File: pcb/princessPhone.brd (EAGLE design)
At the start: 83.8 x 53 mm, 75 parts, among them IC1 OPA2134UA, P2 TC2030-MCP-NL, Q1 2N7002K, SW3 LL1105BF250Q, SW4 LL1105BF250Q, SW5 LL1105BF250Q, SW6 LL1105BF250Q, U1 AG1170-S3-VERTICAL, U2 PI32MX170D-PT, U3 BLUETOOTH-RN-52, U4 V_REG_LD1085D2, X1 22-23-2041, X2 XRJK-S-01-6-4-0-9M2, X3 USB_MICRO_B

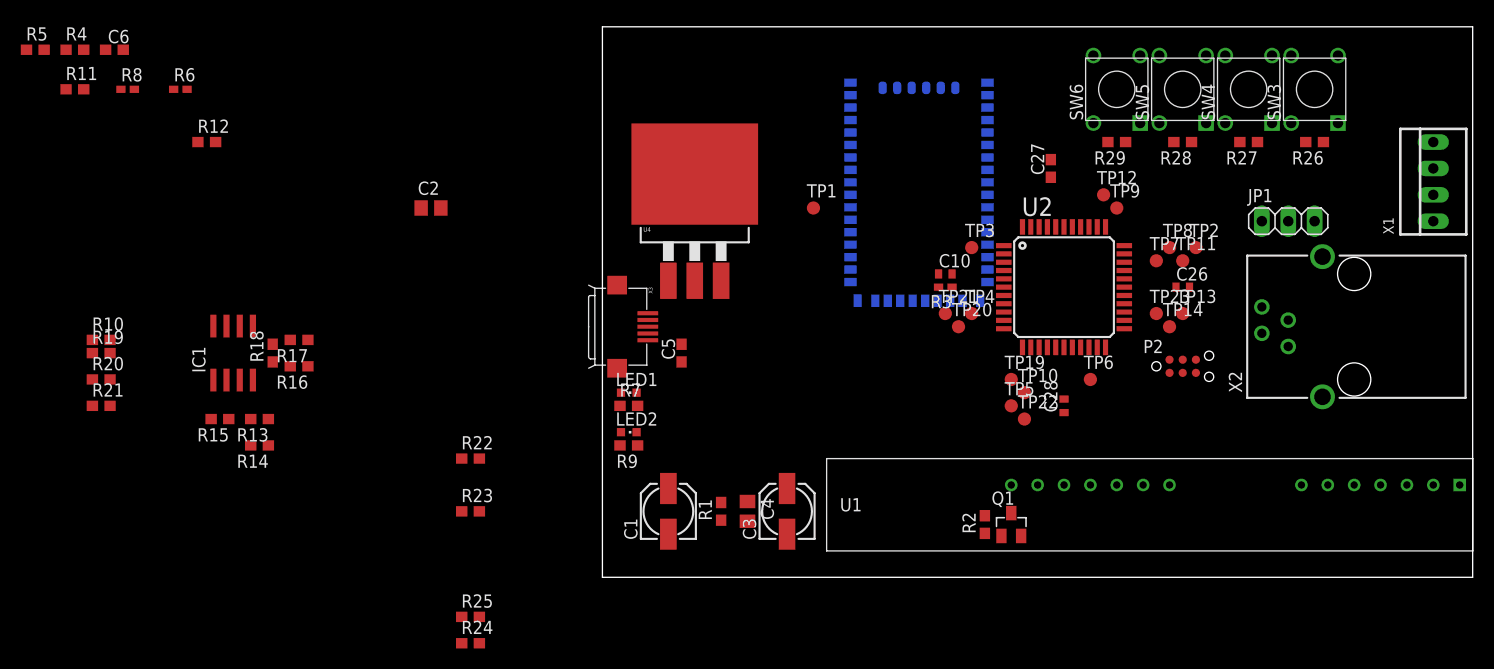
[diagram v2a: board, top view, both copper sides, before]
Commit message: Replaced leo with switcher, finished first-pass layout, added LEDs.
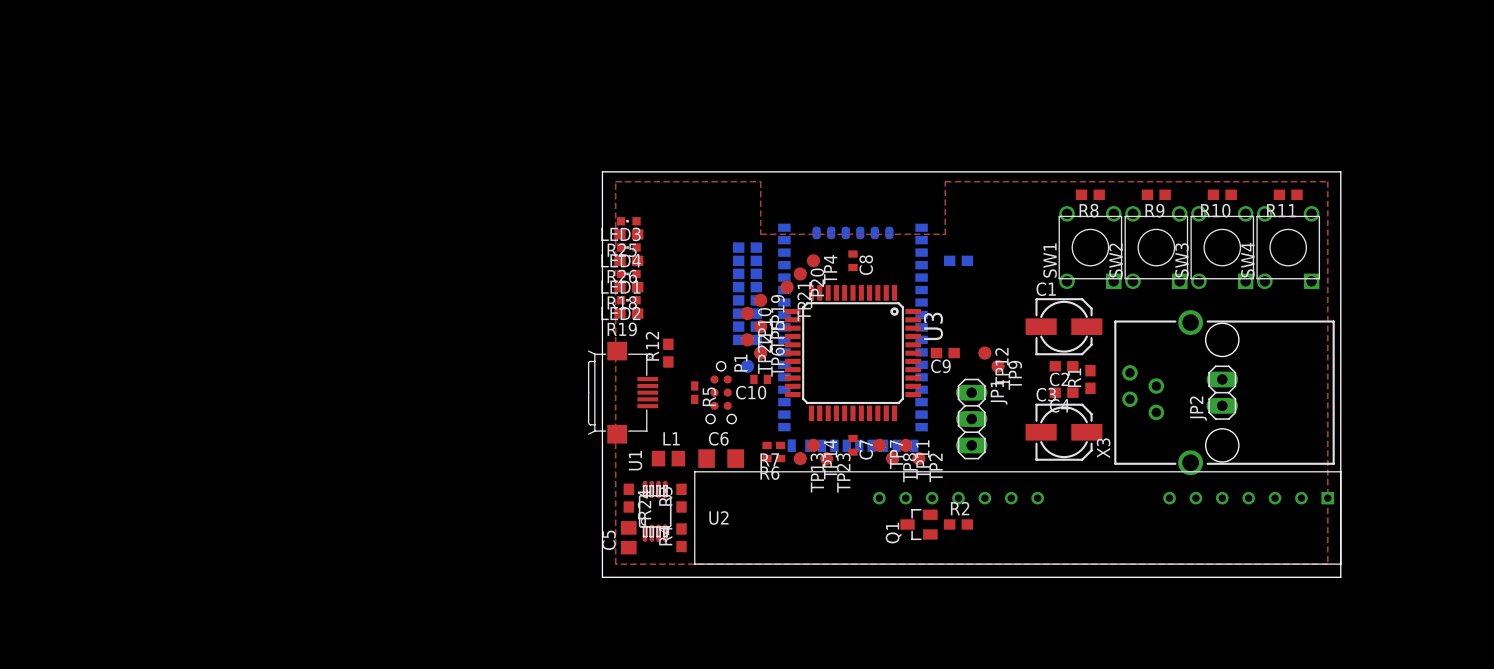
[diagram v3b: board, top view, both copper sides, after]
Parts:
- removed C26: 1UF, rcl:C0402
- removed C27: 10UF, rcl:C0603
- removed C28: 0.1UF, rcl:C0402
- removed IC1: OPA2134UA, linear:SO08
- removed P2: TC2030-MCP-NL, raveGearControl:TC2030-MCP-NL
- removed R27, R28, R29: 10K, rcl:R0603
- removed SW5, SW6: LL1105BF250Q, raveGearControl:LL1105
- removed TP3: PTR1B1,27, testpad:B1,27
- removed X2: XRJK-S-01-6-4-0-9M2, con-xmultiple:XRJK-S-01-6-4-0-9M2
- added C7: 1UF, rcl:C0402
- added C8: 0.1UF, rcl:C0402
- added C9: 10UF, rcl:C0603
- added JP2: (no value), pinhead:1X02
- added L1: 2.2UH, rcl:R0805
- added LED3: BLUE, led:CHIPLED_0603
- added LED4: RED, led:CHIPLED_0603
- added P1: TC2030-MCP-NL, raveGearControl:TC2030-MCP-NL
- added SW1, SW2: LL1105BF250Q, raveGearControl:LL1105
- C2, C4: device rcl:C0805 -> rcl:C0603
- C5: value (none) -> 10UF; device rcl:C0603 -> rcl:C0805
- C6: value (none) -> 22UF; device rcl:C0603 -> rcl:C1206
- R10: value NP -> 10K
- R11: value 47K -> 10K
- R13: value NP -> 47K
- R14, R20, R21: value NP -> 0
- R15, R16, R17: value 47 -> 0
- R19: value NP -> 470
- R24: value 0 -> 100K
- R25: value 0 -> 47
- R26: value 10K -> 470
- R3: value 10K -> 562K; device rcl:R0402 -> rcl:R0603
- R4: value (none) -> 180K
- R5: value (none) -> 10K; device rcl:R0603 -> rcl:R0402
- R7: value 47 -> 10K; device rcl:R0603 -> rcl:R0402
- R8: device rcl:R0402 -> rcl:R0603
- R9: value 470 -> 10K
- U1: value AG1170-S3-VERTICAL -> Value; device princessPhone:AG1170X-S -> princessPhone:DGK0008A_N
- U2: value PI32MX170D-PT -> AG1170-S3-VERTICAL; device raveGear5:TQFP44 -> princessPhone:AG1170X-S
- U3: value BLUETOOTH-RN-52 -> PI32MX170D-PT; device SparkFun-RF:RN-52 -> raveGear5:TQFP44
- U4: value V_REG_LD1085D2 -> BLUETOOTH-RN-52; device SparkFun-PowerIC:D2PACK/A -> SparkFun-RF:RN-52
- X1: value 22-23-2041 -> USB_MICRO_B; device con-molex:22-23-2041 -> FosBattery1:USB-MICROB
- X3: value USB_MICRO_B -> XRJK-S-01-6-4-0-9M2; device FosBattery1:USB-MICROB -> con-xmultiple:XRJK-S-01-6-4-0-9M2
- moved R11 117.3 mm to (66.0, 36.8), turned to 180 degrees
- moved R10 108.9 mm to (59.7, 36.8), turned to 180 degrees
- moved R8 93.3 mm to (47.0, 36.8), turned to 180 degrees
- moved X1 81.3 mm to (1.27, 17.8), turned to 270 degrees
- moved R4 75.0 mm to (7.62, 3.81), turned to 90 degrees
- moved R5 71.6 mm to (8.89, 17.8), turned to 270 degrees
- moved C6 70.4 mm to (11.4, 11.4)
- moved R13 69.0 mm to (34.3, 30.5), flipped to the bottom, turned to 0 degrees
- moved R6 67.3 mm to (16.5, 11.4), turned to 180 degrees
- moved R26 67.0 mm to (2.54, 30.5)
- moved C2 62.8 mm to (44.5, 20.3), turned to 180 degrees
- moved R21 62.7 mm to (14.0, 24.1), flipped to the bottom
- moved R20 62.3 mm to (14.0, 22.9), flipped to the bottom
- moved X3 58.8 mm to (59.7, 17.8), turned to 90 degrees
- moved R9 56.2 mm to (53.3, 36.8)
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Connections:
- removed net PIC32_RSVD_10: TP3.TP, U2.1
- removed net RN52_SPKR_SUM: IC1.3, R13.2, R14.2, R15.1
- new net N$5: L1.1, U1.7
- new net N$6: R24.1, U1.8
- new net N$7: LED3.C, R25.2
- new net VIN: U1.2
- net +3V3: now also C7.1, C8.1, L1.2, LED3.A, LED4.A, P1.2, R10.1, R11.1, R24.2, R5.2, R7.2, R8.1, R9.1, U1.6, U2.13, U3.17, U3.28, U3.40, U4.20; no longer C26.1, C28.1, IC1.8, P2.2, R26.1, R27.1, R28.1, R29.1, R4.2, R8.2, U1.13, U2.17, U2.28, U2.40, U3.20, U4.2, U4.TAB
- net AG1170_AUDIO_IN: now also U2.9; no longer IC1.1, R15.2, U1.9
- net AG1170_AUDIO_OUT: now also R20.2, R21.2, U2.10; no longer IC1.5, R18.2, R24.2, R25.2, U1.10
- net AG1170_F/R: now also U2.3, U3.37; no longer U1.3, U2.37
- net AG1170_PD: now also U3.2; no longer U2.2
- net AG1170_RM: now also U2.4, U3.36; no longer U1.4, U2.36
- net AG1170_SHK: now also U2.5, U3.38; no longer U1.5, U2.38
- net GND: now also C7.2, C8.2, C9.2, P1.3, R13.1, R14.2, R15.2, R16.2, R17.2, R4.1, SW1.1, SW2.1, U1.1, U1.4, U2.12, U3.16, U3.29, U3.39, U3.6, U4.36, U4.G1, U4.G2, U4.G3, U4.G4, U4.RFG1, U4.RFG2, U4.RFG3, U4.RFG4, U4.RFG5, U4.RFG6, X1.GND; no longer C26.2, C27.2, C28.2, IC1.2, IC1.4, IC1.6, P2.3, R10.2, R11.1, R19.2, R20.2, R21.2, R5.1, SW5.1, SW6.1, U1.12, U2.16, U2.29, U2.39, U2.6, U3.36, U3.G1, U3.G2, U3.G3, U3.G4, U3.RFG1, U3.RFG2, U3.RFG3, U3.RFG4, U3.RFG5, U3.RFG6, X3.GND
- net LED0: now also R18.1, U4.30; no longer R7.1, U3.30
- net LED1: now also R19.1, U4.29; no longer R9.1, U3.29
- net MCLR#: now also P1.1, R5.1, U3.18; no longer P2.1, R3.1, U2.18
- net N$1: now also U2.11; no longer U1.11
- net N$10: now also R19.2; no longer R9.2
- net N$11: now also U4.31; no longer U3.31
- net N$12: now also LED4.C, R26.2; no longer IC1.7, R16.2, R17.2, R18.1
- net N$3: now also U2.14; no longer U1.14
- net N$4: now also C9.1, U3.7; no longer C27.1, U2.7
- net N$8: now also R3.1, R4.2, U1.5; no longer R4.1, R5.2, U4.1
- net N$9: now also R18.2; no longer R7.2
- net PHONE_RING: now also JP2.1, U2.1, X3.2; no longer U1.1, X1.1, X2.2
- net PHONE_TIP: now also JP2.2, U2.2, X3.3; no longer U1.2, X1.2, X2.3
- net PIC32_PGEC1: now also P1.5, U3.22; no longer P2.5, U2.22
- net PIC32_PGED1: now also P1.4, U3.21; no longer P2.4, U2.21
- net PIC32_RSVD_1: now also U3.19; no longer U2.19
- net PIC32_RSVD_11: now also U3.9; no longer U2.9
- net PIC32_RSVD_12: now also U3.14; no longer U2.14
- net PIC32_RSVD_2: now also U3.30; no longer U2.30
- net PIC32_RSVD_3: now also U3.31; no longer U2.31
- net PIC32_RSVD_4: now also U3.34; no longer U2.34
- net PIC32_RSVD_5: now also R26.1, U3.13; no longer U2.13
- net PIC32_RSVD_6: now also U3.32; no longer U2.32
- net PIC32_RSVD_7: now also U3.35; no longer U2.35
- net PIC32_RSVD_8: now also R25.1, U3.12; no longer U2.12
- net PIC32_RSVD_9: now also U3.33; no longer U2.33
- net PIC32_SCL2: now also R7.1, U3.24; no longer R8.1, U2.24
- net PIC32_SDA2: now also U3.23; no longer U2.23
- net PIC32_U1CTS#_3V3: now also U3.20, U4.13; no longer U2.20, U3.13
- net PIC32_U1RTS#_3V3: now also U3.8, U4.14; no longer U2.8, U3.14
- net PIC32_U1RX_3V3: now also U3.26, U4.15; no longer U2.26, U3.15
- net PIC32_U1TX_3V3: now also U3.25, U4.16; no longer U2.25, U3.16
- net RN52_CMD_MODE#: now also U3.5, U4.10; no longer U2.5, U3.10
- net RN52_DFU_MODE: now also R13.2, U4.1; no longer R11.2
- net RN52_EVENT#: now also U3.4, U4.2; no longer U2.4, U3.2
- net RN52_FACTORY_RST: now also U4.4; no longer U3.4
- net RN52_MIC_L+: now also R20.1, U4.32; no longer R16.1, R24.1, R25.1, U3.32
- net RN52_MIC_L-: now also R17.1, U4.34; no longer R21.1, U3.34
- net RN52_MIC_R+: now also R21.1, U4.33; no longer R17.1, U3.33
- net RN52_MIC_R-: now also R16.1, U4.35; no longer R20.1, U3.35
- net RN52_PWREN: now also U3.3, U4.19; no longer U2.3, U3.19
- net RN52_SPKR_L+: now also U4.40; no longer R13.1, U3.40
- net RN52_SPKR_L-: now also R14.1, U4.38; no longer R10.1, U3.38
- net RN52_SPKR_R+: now also U4.39; no longer R14.1, U3.39
- net RN52_SPKR_R-: now also R15.1, U4.37; no longer R19.1, U3.37
- net SST25_CE#: now also U3.10; no longer U2.10
- net SST25_MISO: now also U3.27; no longer U2.27
- net SST25_MOSI: now also U3.11; no longer U2.11
- net SST25_SCK: now also U3.15; no longer U2.15
- net SW0: now also R8.2, SW1.3, U3.41; no longer R26.2, SW3.3, U2.41
- net SW1: now also R9.2, SW2.3, U3.42; no longer R27.2, SW4.3, U2.42
- net SW2: now also R10.2, SW3.3, U3.43; no longer R28.2, SW5.3, U2.43
- net SW3: now also R11.2, SW4.3, U3.44; no longer R29.2, SW6.3, U2.44
- net USB_DM: now also U4.11, X1.D-; no longer U3.11, X3.D-
- net USB_DP: now also U4.12, X1.D+; no longer U3.12, X3.D+
- net USB_VBUS: now also U1.3, X1.VBUS; no longer U4.3, X3.VBUS
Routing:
- added copper zone on layer 1, net +3V3
- added copper zone on layer 16, net GND
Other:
- board size 83.8 x 53 mm -> 71.1 x 39 mm

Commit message: FIRST PASS AT LAYOUT
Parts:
- removed TP4: PTR1B1,27, testpad:B1,27
- added TP3: PTR1B1,27, testpad:B1,27
- JP1: device pinhead:1X03 -> pinhead:1X04
- LED3: value BLUE -> GREEN
- LED4: value RED -> YELLOW
- R25: value 47 -> 150
- R26: value 470 -> 150
- moved C9 14.5 mm to (21.6, 30.5)
- moved TP9 7.10 mm to (31.8, 17.1)
- moved TP12 5.46 mm to (33.7, 17.1)
- moved R22 3.48 mm to (10.8, 33.2)
- moved L1 3.24 mm to (3.17, 10.8), turned to 180 degrees
- moved R23 3.21 mm to (10.8, 31.1)
- moved LED3 3.18 mm to (2.54, 37.5)
- moved C10 3.18 mm to (15.2, 15.9)
- moved C6 3.17 mm to (8.26, 11.4)
- moved TP23 2.69 mm to (23.5, 13.3)
- moved R25 2.54 mm to (2.54, 35.6)
- moved R20 2.44 mm to (14.0, 20.4)
- moved C7 2.19 mm to (25.5, 10.9), turned to 180 degrees
- moved TP1 2.06 mm to (14.4, 18.3)
- moved LED4 1.91 mm to (2.54, 33.7)
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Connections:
- removed net AG1170_AUDIO_IN_AGG: R22.1, R23.2
- removed net PIC32_RSVD_11: TP4.TP, U3.9
- removed net VIN: U1.2
- net +3V3: now also JP1.1
- net AG1170_AUDIO_IN: now also R22.1, R23.2
- net GND: now also JP1.4; no longer JP1.1
- net PHONE_RING: now also X3.3; no longer X3.2
- net PHONE_TIP: now also X3.2; no longer X3.3
- net PIC32_U1RX_3V3: now also JP1.3; no longer JP1.2
- net PIC32_U1TX_3V3: now also JP1.2; no longer JP1.3
- net RN52_FACTORY_RST: now also U3.9
- net RN52_SPKR_R+: now also TP3.TP
- net USB_VBUS: now also U1.2
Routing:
- net RN52_DFU_MODE: track 0.00 -> 48.4 mm, vias 0 -> 5
- net AG1170_F/R: track 0.00 -> 47.4 mm, vias 0 -> 2
- net GND: track 0.00 -> 46.8 mm, vias 0 -> 12
- net AG1170_SHK: track 0.00 -> 45.2 mm, vias 0 -> 2
- net AG1170_RM: track 0.00 -> 44.6 mm, vias 0 -> 2
- net AG1170_PD: track 0.00 -> 32.1 mm, vias 0 -> 2
- net PIC32_U1RX_3V3: track 0.00 -> 28.6 mm, vias 0 -> 2
- net N$1: track 0.00 -> 27.3 mm, vias 0 -> 2
- net USB_VBUS: track 0.00 -> 26.0 mm, vias 0 -> 2
- net PIC32_U1TX_3V3: track 0.00 -> 25.7 mm, vias 0 -> 2
- net PHONE_TIP: track 0.00 -> 25.1 mm
- net PHONE_RING: track 0.00 -> 23.4 mm
- net PIC32_U1RTS#_3V3: track 0.00 -> 16.9 mm, vias 0 -> 1
- net PIC32_U1CTS#_3V3: track 0.00 -> 15.3 mm, vias 0 -> 1
- net RN52_PWREN: track 0.00 -> 15.0 mm, vias 0 -> 1
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
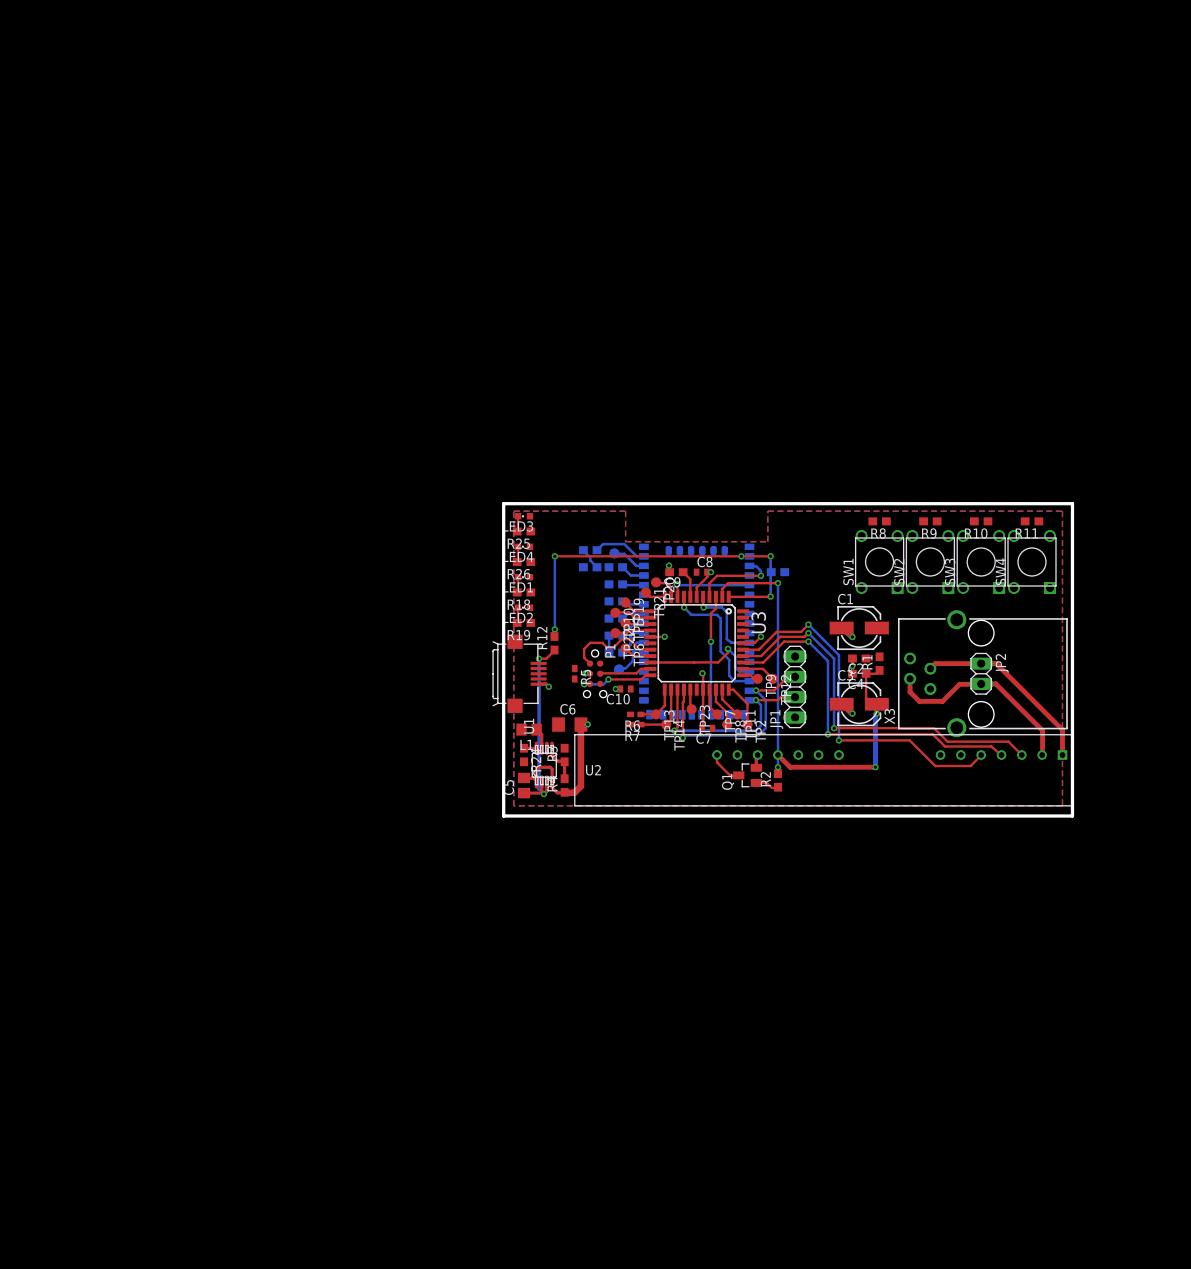
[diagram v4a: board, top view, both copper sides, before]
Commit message: REMOVED BTN, ADDING LEDS, ADDED OUTLINE
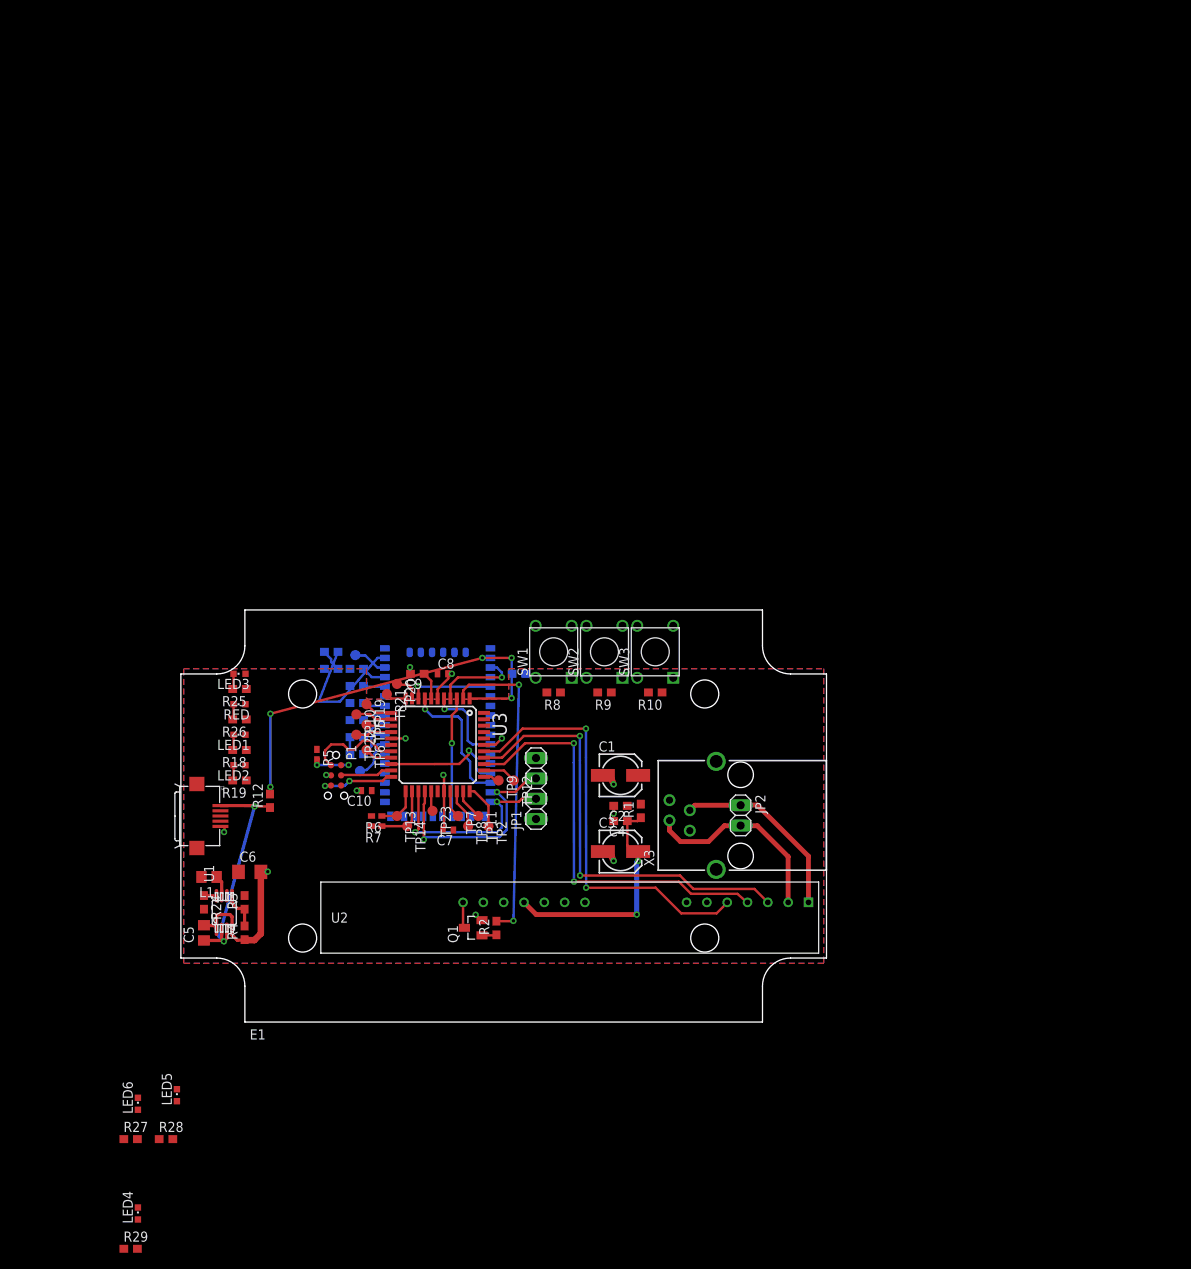
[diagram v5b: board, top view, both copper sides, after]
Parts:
- removed R11: 10K, rcl:R0603
- removed SW4: LL1105BF250Q, raveGearControl:LL1105
- added E1: 1591XXMS, princessPhone:1591XXMSBK
- added LED5: GREEN, led:CHIPLED_0603
- added LED6, RED: YELLOW, led:CHIPLED_0603
- added R27, R28, R29: 150, rcl:R0603
- moved LED4 96.3 mm to (-45.7, -49.7), turned to 0 degrees
- moved R8 46.0 mm to (6.25, 15.4)
- moved R9 46.0 mm to (12.6, 15.4)
- moved R10 46.0 mm to (18.9, 15.4)
- moved C5 44.0 mm to (-37.5, -14.6)
- moved C6 44.0 mm to (-31.8, -6.99)
- moved R24 44.0 mm to (-37.5, -10.8)
- moved L1 44.0 mm to (-36.8, -7.62)
- moved R3 44.0 mm to (-32.4, -10.8)
- moved R4 44.0 mm to (-32.4, -14.6)
- moved U1 44.0 mm to (-34.9, -12.1)
- moved X1 43.6 mm to (-38.5, 0.00)
- moved SW1 42.3 mm to (6.25, 20.5)
- moved SW2 42.3 mm to (12.6, 20.5)
- moved SW3 42.3 mm to (18.9, 20.5)
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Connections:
- net N$1 renamed +VA
- new net +3V1: LED5.A
- new net N$1: LED5.C, R27.2
- new net N$13: LED6.C, R28.2
- new net N$14: LED4.C, R29.2
- net +3V3: now also RED.A; no longer LED4.A, R11.1
- net GND: no longer SW4.1
- net N$12: now also RED.C; no longer LED4.C
- net PIC32_RSVD_5: now also R28.1, R29.1
- net PIC32_RSVD_8: now also R27.1
- net SW3: no longer R11.2, SW4.3
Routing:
- net RN52_SPKR_L+: track 6.81 -> 17.5 mm
- net AG1170_SHK: track 45.2 -> 53.4 mm
- net AG1170_F/R: track 47.4 -> 55.4 mm
- net AG1170_PD: track 32.1 -> 39.9 mm
- net AG1170_RM: track 44.6 -> 52.3 mm
- net +3V3: track 0.00 -> 5.03 mm, vias 0 -> 2
- net RN52_DFU_MODE: track 48.4 -> 52.5 mm
- net USB_VBUS: track 26.0 -> 30.0 mm
- net +VA: track 27.3 -> 29.2 mm
- net N$2: track 3.01 -> 1.83 mm
- net N$3: track 4.34 -> 3.25 mm
- net GND: track 46.8 -> 46.5 mm, vias 12 -> 13
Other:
- board size 71.1 x 39 mm -> 80.7 x 51.5 mm
